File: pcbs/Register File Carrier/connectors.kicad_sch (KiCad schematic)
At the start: 2 parts

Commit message: Roughing a little more out
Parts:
- added J2003, J2004: ~, BoardEdgeConnectors:TE-5530843-4-Mount, symbol BoardEdgeConnectors:TE-5530843-4
- added U2001: 74AHC04, Package_SO:SOIC-14_3.9x8.7mm_P1.27mm, symbol 74xx:74AHC04
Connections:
- net +5V: now also J2003.B1, J2004.B1, U2001.14 (VCC)
- net A0: now also J2003.A10
- net A1: now also J2003.B10
- net A10: now also J2004.A11
- net A11: now also J2004.B11
- net A12: now also J2004.A12
- net A13: now also J2004.B12
- net A14: now also J2004.A13
- net A15: now also J2004.B13
- net A2: now also J2003.A11
- net A3: now also J2003.B11
- net A4: now also J2003.A12
- net A5: now also J2003.B12
- net A6: now also J2003.A13
- net A7: now also J2003.B13
- net A8: now also J2004.A10
- net A9: now also J2004.B10
- net B0: now also J2003.A14
- net B1: now also J2003.B14
- net B10: now also J2004.A15
- net B11: now also J2004.B15
- net B12: now also J2004.A16
- net B13: now also J2004.B16
- net B14: now also J2004.A17
- net B15: now also J2004.B17
- net B2: now also J2003.A15
- net B3: now also J2003.B15
- net B4: now also J2003.A16
- net B5: now also J2003.B16
- net B6: now also J2003.A17
- net B7: now also J2003.B17
- net B8: now also J2004.A14
- net B9: now also J2004.B14
- net C0: now also J2003.A18
- net C1: now also J2003.B18
- net C10: now also J2004.A19
- net C11: now also J2004.B19
- net C12: now also J2004.A20
- net C13: now also J2004.B20
- net C14: now also J2004.A21
- net C15: now also J2004.B21
- net C2: now also J2003.A19
- net C3: now also J2003.B19
- net C4: now also J2003.A20
- net C5: now also J2003.B20
- net C6: now also J2003.A21
- net C7: now also J2003.B21
- net C8: now also J2004.A18
- net C9: now also J2004.B18
- net CLK: now also J2003.B4, J2004.B4
- net GND: now also J2003.A22, J2004.A22, U2001.11, U2001.13, U2001.7 (GND), U2001.9
- net R_{A}0: now also J2003.A7, J2004.A7
- net R_{A}1: now also J2003.B7, J2004.B7
- net R_{A}2: now also J2003.A8, J2004.A8
- net R_{A}3: now also U2001.1
- net R_{B}0: now also J2003.A5, J2004.A5
- net R_{B}1: now also J2003.B5, J2004.B5
- net R_{B}2: now also J2003.A6, J2004.A6
- net R_{B}3: now also U2001.3
- net R_{C}0: now also J2003.A2, J2004.A2
- net R_{C}1: now also J2003.B2, J2004.B2
- net R_{C}2: now also J2003.A3, J2004.A3
- net R_{C}3: now also U2001.5
- net ~{Active}: now also J2003.A4, J2004.A4
- new net ~{R_{A}3}: J2003.B8, J2004.B8, U2001.2
- new net ~{R_{B}3}: J2003.B6, J2004.B6, U2001.4
- new net ~{R_{C}3}: J2003.B3, J2004.B3, U2001.6
- no-connect marks 8 -> 19
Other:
- note added: "Registers 8-15"

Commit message: Lots of routing
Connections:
- net GND: now also U2001.3; no longer U2001.11
- net R_{B}3: now also U2001.11; no longer U2001.3
- net ~{R_{B}3}: now also U2001.10; no longer U2001.4
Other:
- moved on the sheet: U2001B, U2001E
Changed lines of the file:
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@@
 	(symbol
 		(lib_id "74xx:74AHC04")
-		(at 152.4 162.56 0)
+		(at 83.82 147.32 0)
 		(unit 5)
 		(exclude_from_sim no)
@@
 		(fields_autoplaced yes)
 		(property "Reference" "U2001"
-			(at 152.4 153.67 0)
+			(at 83.82 138.43 0)
 			(effects
 				(font
@@
 		)
 		(property "Value" "74AHC04"
-			(at 152.4 156.21 0)
+			(at 83.82 140.97 0)
 			(effects
 				(font
@@
 		)
 		(property "Footprint" "Package_SO:SOIC-14_3.9x8.7mm_P1.27mm"
-			(at 152.4 162.56 0)
+			(at 83.82 147.32 0)
 			(effects
 				(font
@@
 		)
 		(property "Datasheet" "https://assets.nexperia.com/documents/data-sheet/74AHC_AHCT04.pdf"
-			(at 152.4 162.56 0)
+			(at 83.82 147.32 0)
 			(effects
 				(font
@@
 		)
 		(property "Description" "Hex Inverter"
-			(at 152.4 162.56 0)
+			(at 83.82 147.32 0)
 			(effects
 				(font
@@
 		)
 		(property "LCSC" "C5590"
-			(at 152.4 162.56 0)
+			(at 83.82 147.32 0)
 			(effects
 				(font
@@
 	(symbol
 		(lib_id "74xx:74AHC04")
-		(at 83.82 147.32 0)
+		(at 152.4 162.56 0)
 		(unit 2)
 		(exclude_from_sim no)
@@
 		(fields_autoplaced yes)
 		(property "Reference" "U2001"
-			(at 83.82 138.43 0)
+			(at 152.4 153.67 0)
 			(effects
 				(font
@@
 		)
 		(property "Value" "74AHC04"
-			(at 83.82 140.97 0)
+			(at 152.4 156.21 0)
 			(effects
 				(font
@@
 		)
 		(property "Footprint" "Package_SO:SOIC-14_3.9x8.7mm_P1.27mm"
-			(at 83.82 147.32 0)
+			(at 152.4 162.56 0)
 			(effects
 				(font
@@
 		)
 		(property "Datasheet" "https://assets.nexperia.com/documents/data-sheet/74AHC_AHCT04.pdf"
-			(at 83.82 147.32 0)
+			(at 152.4 162.56 0)
 			(effects
 				(font
@@
 		)
 		(property "Description" "Hex Inverter"
-			(at 83.82 147.32 0)
+			(at 152.4 162.56 0)
 			(effects
 				(font
@@
 		)
 		(property "LCSC" "C5590"
-			(at 83.82 147.32 0)
-			(effects
-				(font
+			(at 152.4 162.56 0)
+			(effects
+				(font

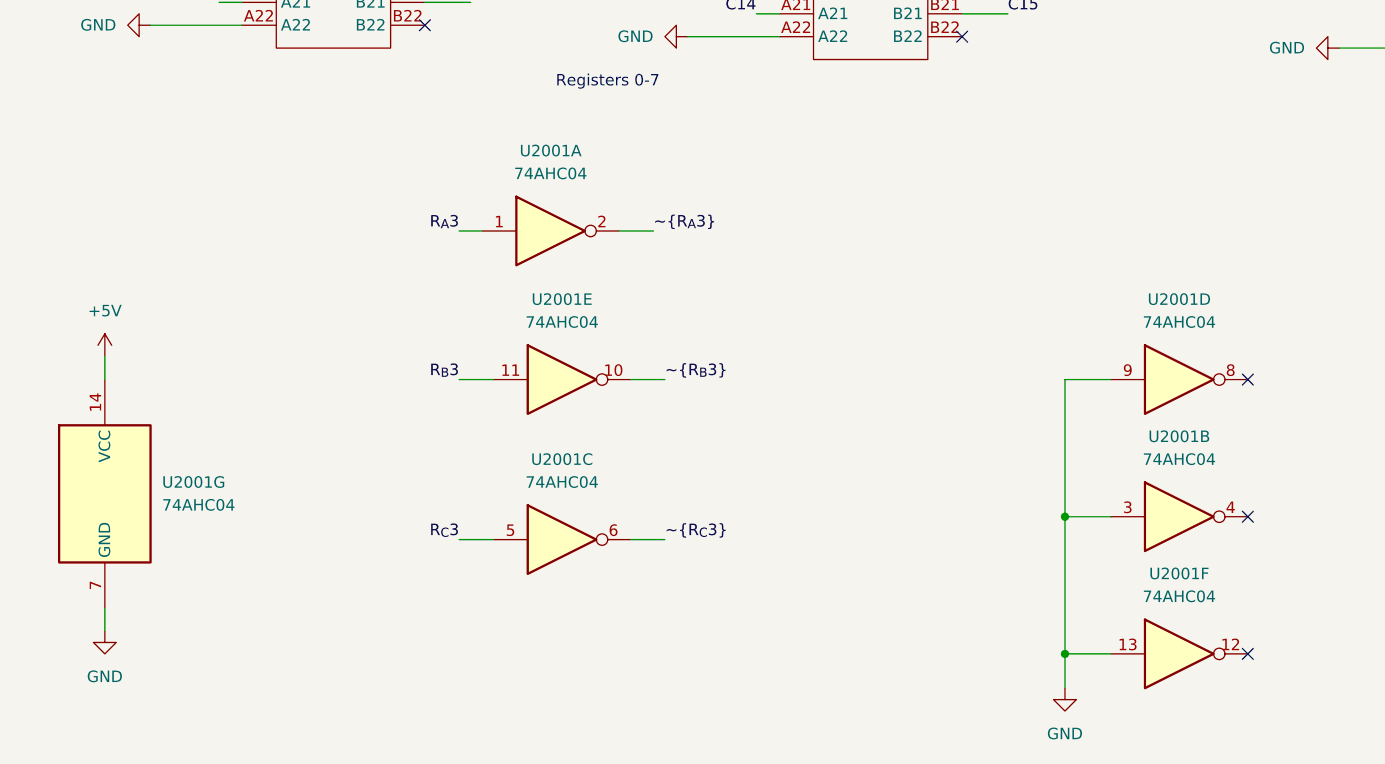
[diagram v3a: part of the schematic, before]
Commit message: [PCB] Register File Carrier r01 (#21)
Update the Register File Carrier to get the 'enable' logic correct. Had constructed an 'Active High' when 'Active Low' was required.

Also should address #20 , standardising on a single part.
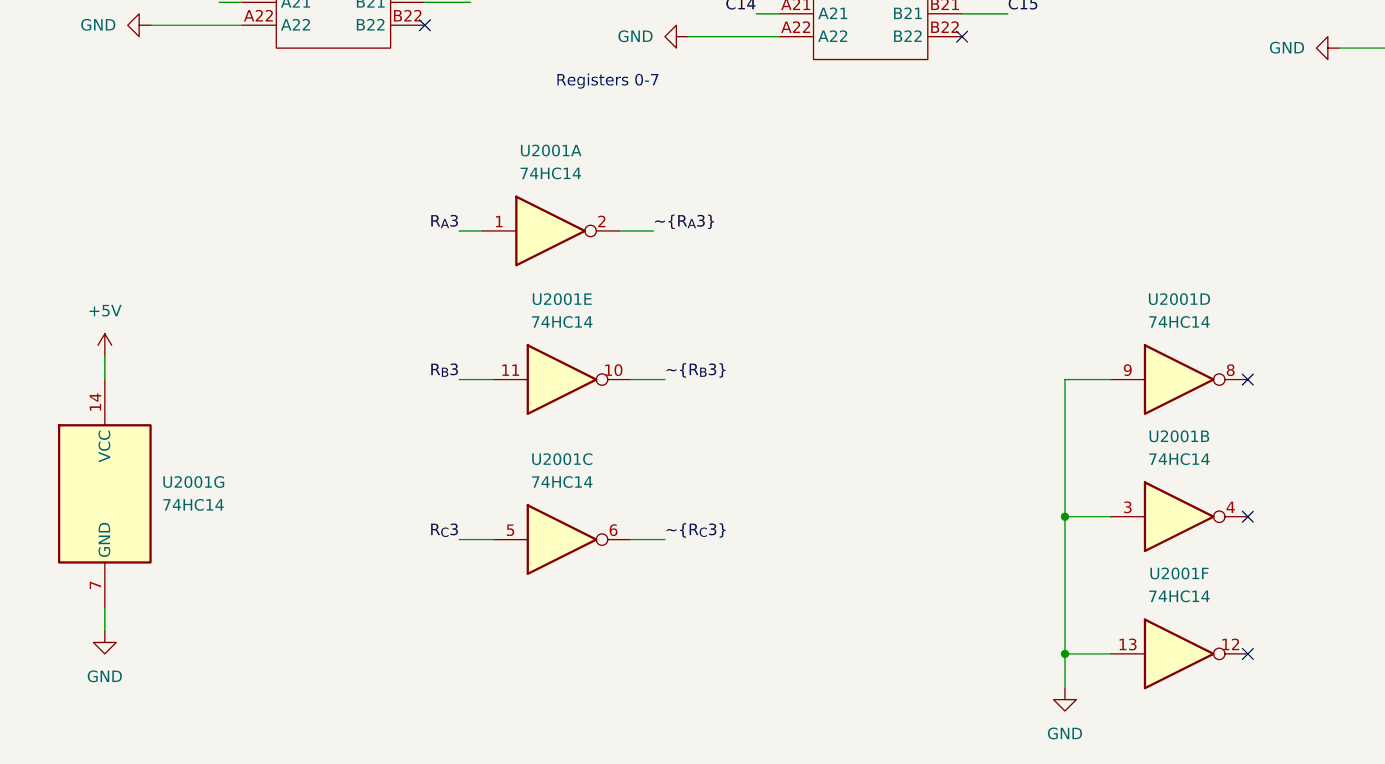
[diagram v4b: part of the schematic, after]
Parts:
- U2001: value 74AHC04 -> 74HC14; LCSC C5590 -> C5605
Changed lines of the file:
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@@
 			)
 		)
-		(property "Value" "74AHC04"
+		(property "Value" "74HC14"
 			(at 83.82 158.75 0)
 			(effects
@@
 			)
 		)
-		(property "Datasheet" "https://assets.nexperia.com/documents/data-sheet/74AHC_AHCT04.pdf"
+		(property "Datasheet" "https://jlcpcb.com/api/file/downloadByFileSystemAccessId/8579708675566587904"
 			(at 83.82 165.1 0)
 			(effects
@@
 			)
 		)
-		(property "LCSC" "C5590"
+		(property "LCSC" "C5605"
 			(at 83.82 165.1 0)
 			(effects
@@
 			)
 		)
-		(property "Value" "74AHC04"
+		(property "Value" "74HC14"
 			(at 83.82 140.97 0)
 			(effects
@@
 			)
 		)
-		(property "Datasheet" "https://assets.nexperia.com/documents/data-sheet/74AHC_AHCT04.pdf"
+		(property "Datasheet" "https://jlcpcb.com/api/file/downloadByFileSystemAccessId/8579708675566587904"
 			(at 83.82 147.32 0)
 			(effects
@@
 			)
 		)
-		(property "LCSC" "C5590"
+		(property "LCSC" "C5605"
 			(at 83.82 147.32 0)
 			(effects
@@
 			)
 		)
-		(property "Value" "74AHC04"
+		(property "Value" "74HC14"
 			(at 152.4 156.21 0)
 			(effects
@@
 			)
 		)
-		(property "Datasheet" "https://assets.nexperia.com/documents/data-sheet/74AHC_AHCT04.pdf"
+		(property "Datasheet" "https://jlcpcb.com/api/file/downloadByFileSystemAccessId/8579708675566587904"
 			(at 152.4 162.56 0)
 			(effects
@@
 			)
 		)
-		(property "LCSC" "C5590"
+		(property "LCSC" "C5605"
 			(at 152.4 162.56 0)
 			(effects
@@
 			)
 		)
-		(property "Value" "74AHC04"
+		(property "Value" "74HC14"
 			(at 152.4 140.97 0)
 			(effects
@@
 			)
 		)
-		(property "Datasheet" "https://assets.nexperia.com/documents/data-sheet/74AHC_AHCT04.pdf"
+		(property "Datasheet" "https://jlcpcb.com/api/file/downloadByFileSystemAccessId/8579708675566587904"
 			(at 152.4 147.32 0)
 			(effects
@@
 			)
 		)
-		(property "LCSC" "C5590"
+		(property "LCSC" "C5605"
 			(at 152.4 147.32 0)
 			(effects
@@
 			)
 		)
-		(property "Value" "74AHC04"
+		(property "Value" "74HC14"
 			(at 39.37 161.2899 0)
 			(effects
@@
 			)
 		)
-		(property "Datasheet" "https://assets.nexperia.com/documents/data-sheet/74AHC_AHCT04.pdf"
+		(property "Datasheet" "https://jlcpcb.com/api/file/downloadByFileSystemAccessId/8579708675566587904"
 			(at 33.02 160.02 0)
 			(effects
@@
 			)
 		)
-		(property "LCSC" "C5590"
+		(property "LCSC" "C5605"
 			(at 33.02 160.02 0)
 			(effects
@@
 			)
 		)
-		(property "Value" "74AHC04"
+		(property "Value" "74HC14"
 			(at 82.55 124.46 0)
 			(effects
@@
 			)
 		)
-		(property "Datasheet" "https://assets.nexperia.com/documents/data-sheet/74AHC_AHCT04.pdf"
+		(property "Datasheet" "https://jlcpcb.com/api/file/downloadByFileSystemAccessId/8579708675566587904"
 			(at 82.55 130.81 0)
 			(effects
@@
 			)
 		)
-		(property "LCSC" "C5590"
+		(property "LCSC" "C5605"
 			(at 82.55 130.81 0)
 			(effects
@@
 			)
 		)
-		(property "Value" "74AHC04"
+		(property "Value" "74HC14"
 			(at 152.4 171.45 0)
 			(effects
@@
 			)
 		)
-		(property "Datasheet" "https://assets.nexperia.com/documents/data-sheet/74AHC_AHCT04.pdf"
+		(property "Datasheet" "https://jlcpcb.com/api/file/downloadByFileSystemAccessId/8579708675566587904"
 			(at 152.4 177.8 0)
 			(effects
@@
 			)
 		)
-		(property "LCSC" "C5590"
+		(property "LCSC" "C5605"
 			(at 152.4 177.8 0)
 			(effects
